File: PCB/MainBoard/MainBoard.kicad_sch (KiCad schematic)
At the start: 13 parts, among them J1 Switch, U1 MCP1700-3302E/TO, U2 ATmega4808-A

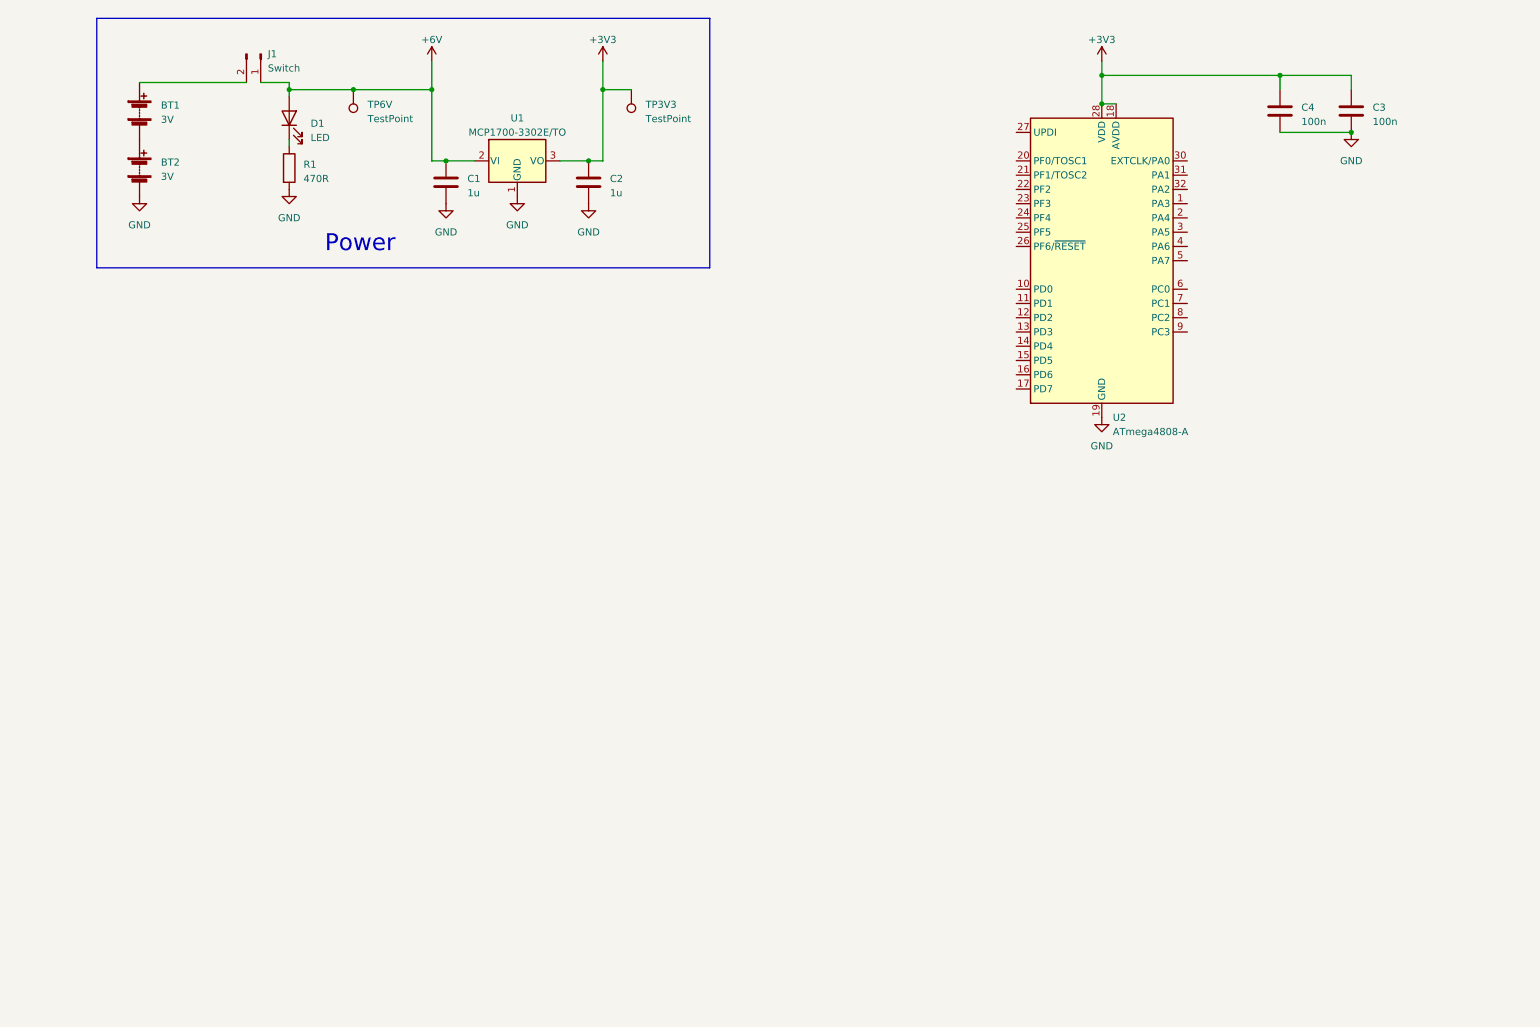
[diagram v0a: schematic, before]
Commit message: Added MCU supporting components
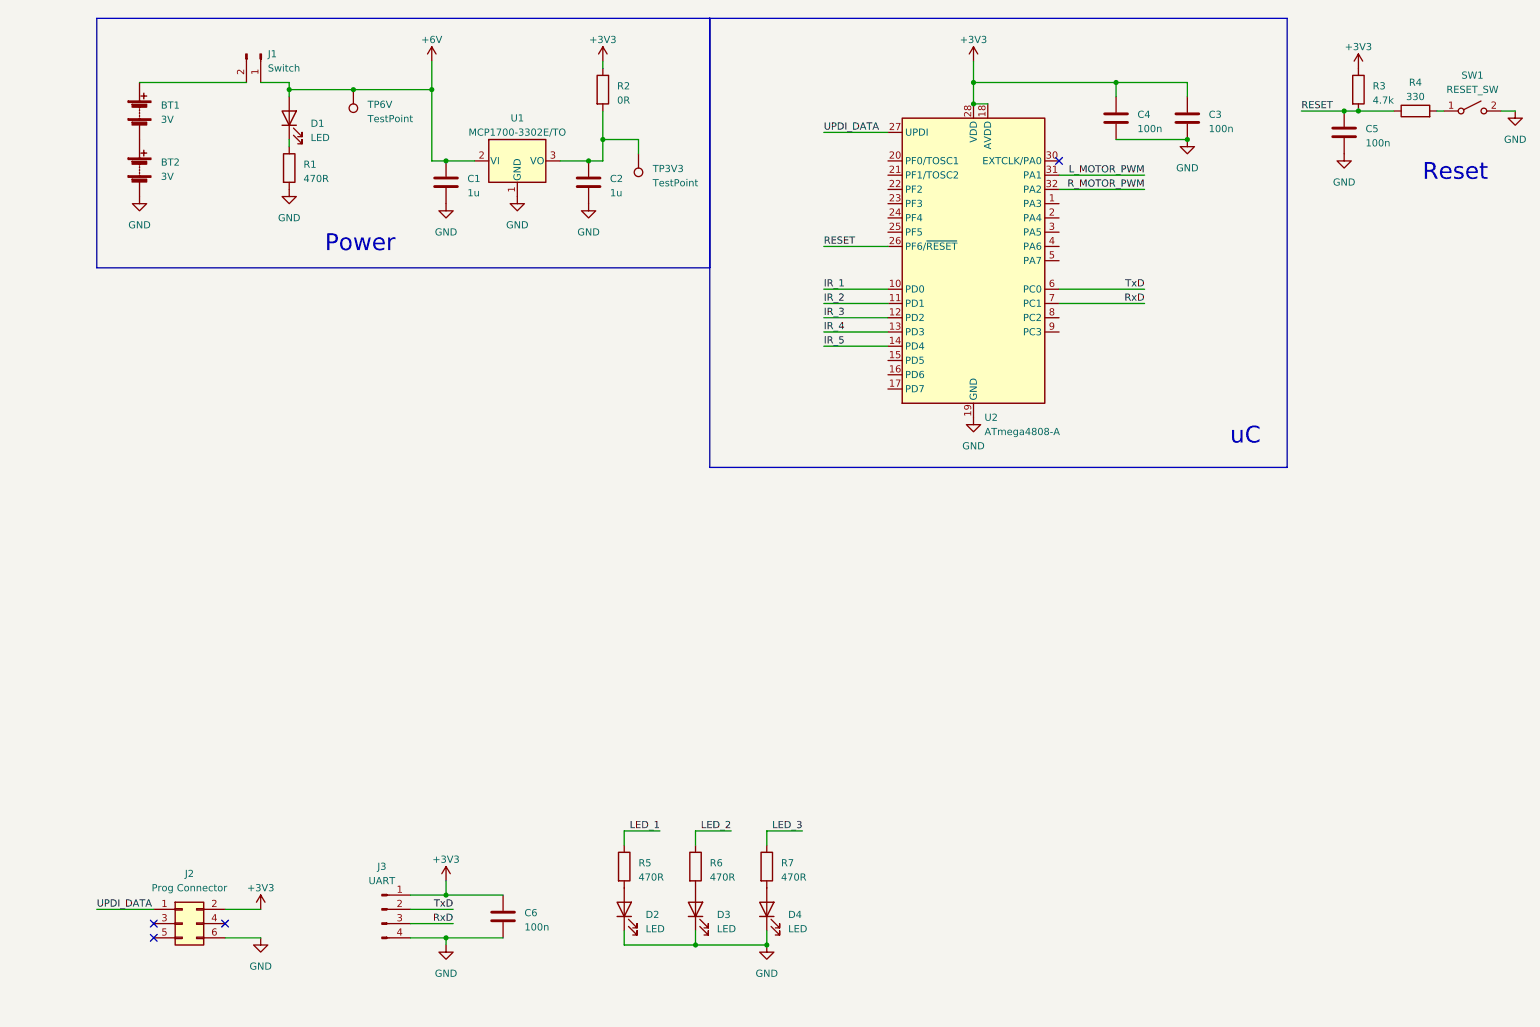
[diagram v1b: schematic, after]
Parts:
- added C5, C6: 100n, symbol Device:C
- added D2, D3, D4: LED, symbol Device:LED
- added J2: Prog Connector, symbol Connector_Generic:Conn_02x03_Odd_Even
- added J3: UART, symbol Connector:Conn_01x04_Pin
- added R2: 0R, symbol Device:R
- added R3: 4.7k, symbol Device:R
- added R4: 330, symbol Device:R
- added R5, R6, R7: 470R, symbol Device:R
- added SW1: RESET_SW, symbol Switch:SW_SPST
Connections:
- net +3V3: now also C6.1, J2.2 (Pin_2), J3.1 (Pin_1), R2.1, R3.1; no longer C2.1, TP3V3.1, U1.3 (VO)
- net GND: now also C5.2, C6.2, D2.1 (K), D3.1 (K), D4.1 (K), J2.6 (Pin_6), J3.4 (Pin_4), SW1.2 (B)
- net IR_1: now reaches U2.10 (PD0)
- net IR_2: now reaches U2.11 (PD1)
- net IR_3: now reaches U2.12 (PD2)
- net IR_4: now reaches U2.13 (PD3)
- net IR_5: now reaches U2.14 (PD4)
- net RESET: now reaches U2.26 (PF6/~{RESET})
- net RESET: now also C5.1, R3.2, R4.1
- net UPDI_DATA: now reaches U2.27 (UPDI)
- net UPDI_DATA: now also J2.1 (Pin_1)
- net L_MOTOR_PWM: now reaches U2.31 (PA1)
- net R_MOTOR_PWM: now reaches U2.32 (PA2)
- net TxD: now reaches U2.6 (PC0)
- net TxD: now also J3.2 (Pin_2)
- net RxD: now reaches U2.7 (PC1)
- net RxD: now also J3.3 (Pin_3)
- new net: C2.1, R2.2, TP3V3.1, U1.3 (VO)
- new net: R4.2, SW1.1 (A)
- new net: D4.2 (A), R7.2
- new net: D2.2 (A), R5.2
- new net: D3.2 (A), R6.2
- new net LED_1: R5.1
- new net LED_2: R6.1
- new net LED_3: R7.1
- no-connect marks 0 -> 4
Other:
- note added: "Reset"
- note added: "uC"
- moved on the sheet: C3, C4, TP3V3, U2

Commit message: Progress on Main Board
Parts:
- added J4: IR Connector, Connector_PinHeader_2.54mm:PinHeader_2x04_P2.54mm_Vertical, symbol PCM_4ms_Connector:Conn_02x04
- added J5, J6: Conn_01x02_Pin, Connector_PinHeader_2.54mm:PinHeader_1x02_P2.54mm_Vertical, symbol Connector:Conn_01x02_Pin
- BT1, BT2: footprint (none) -> Battery:BatteryHolder_Keystone_2462_2xAA
- C1, C2, C3, C4, C5, C6: footprint (none) -> Capacitor_SMD:C_1206_3216Metric
- D1, D2, D3, D4: footprint (none) -> LED_THT:LED_D5.0mm
- J1: footprint (none) -> Connector_PinHeader_2.54mm:PinHeader_1x02_P2.54mm_Vertical
- J2: footprint (none) -> Connector_PinHeader_2.54mm:PinHeader_2x03_P2.54mm_Vertical
- J3: footprint (none) -> Connector_PinHeader_2.54mm:PinHeader_1x04_P2.54mm_Vertical
- R1, R2, R3, R4, R5, R6, R7: footprint (none) -> Resistor_SMD:R_1206_3216Metric
- SW1: footprint (none) -> Button_Switch_THT:SW_PUSH_6mm
- TP3V3: footprint (none) -> TestPoint:TestPoint_Pad_D2.0mm
- TP6V1: renamed from TP6V; footprint (none) -> TestPoint:TestPoint_Pad_D2.0mm
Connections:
- net GND: now also J4.8 (Pin_8), J5.2 (Pin_2), J6.2 (Pin_2)
- net IR_1: now also J4.3 (Pin_3)
- net IR_2: now also J4.5 (Pin_5)
- net IR_3: now also J4.7 (Pin_7)
- net IR_4: now also J4.4 (Pin_4)
- net IR_5: now also J4.6 (Pin_6)
- new net L_MotorOut: J5.1 (Pin_1)
- new net R_MotorOut: J6.1 (Pin_1)
- new net VCC: J4.1 (Pin_1)
- no-connect marks 4 -> 5

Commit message: More main
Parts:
- added C7, C8: 10u, Capacitor_SMD:C_1206_3216Metric, symbol Device:C
- added D1 (x2): SB130, Diode_THT:D_DO-41_SOD81_P7.62mm_Horizontal, symbol Diode:SB130
- added J7, J8: Conn_01x02_Pin, Connector_PinHeader_2.54mm:PinHeader_1x02_P2.54mm_Vertical, symbol Connector:Conn_01x02_Pin
- added Q2 (x2): BSR802, Package_TO_SOT_SMD:SOT-23, symbol Transistor_FET:2N7002H
- added R1 (x2): 10000, Resistor_SMD:R_0805_2012Metric, symbol Device:R
- added R2 (x2): 100, Resistor_SMD:R_0805_2012Metric, symbol Device:R
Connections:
- net +6V: now also C7.1, C8.1, D1.1 (K), D1.1 (K), J7.2 (Pin_2), J8.2 (Pin_2)
- net GND: now also C7.2, C8.2, Q2.2 (S), Q2.2 (S), R1.2, R1.2
- net L_MOTOR_PWM: now also R1.1, R2.1
- net R_MOTOR_PWM: now also R1.1, R2.1
- new net: Q2.1 (G), R2.2 (x2)
- new net: D1.2 (A), J7.1 (Pin_1), Q2.3 (D)
- new net: D1.2 (A), J8.1 (Pin_1), Q2.3 (D)

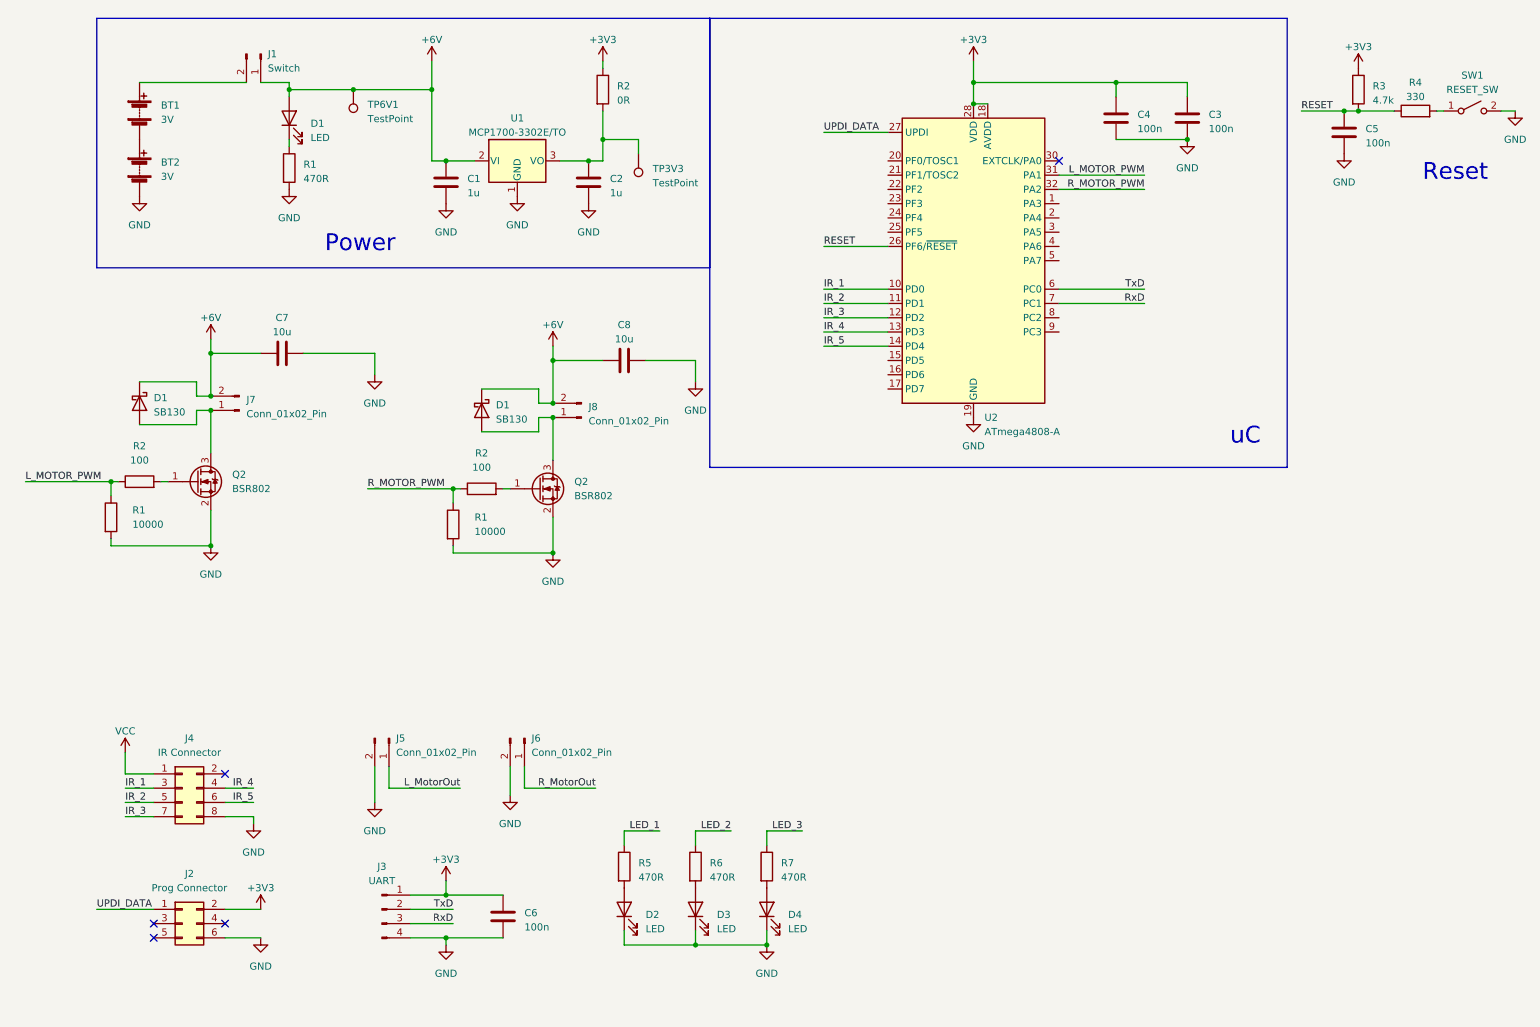
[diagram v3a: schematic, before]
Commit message: Routed main board
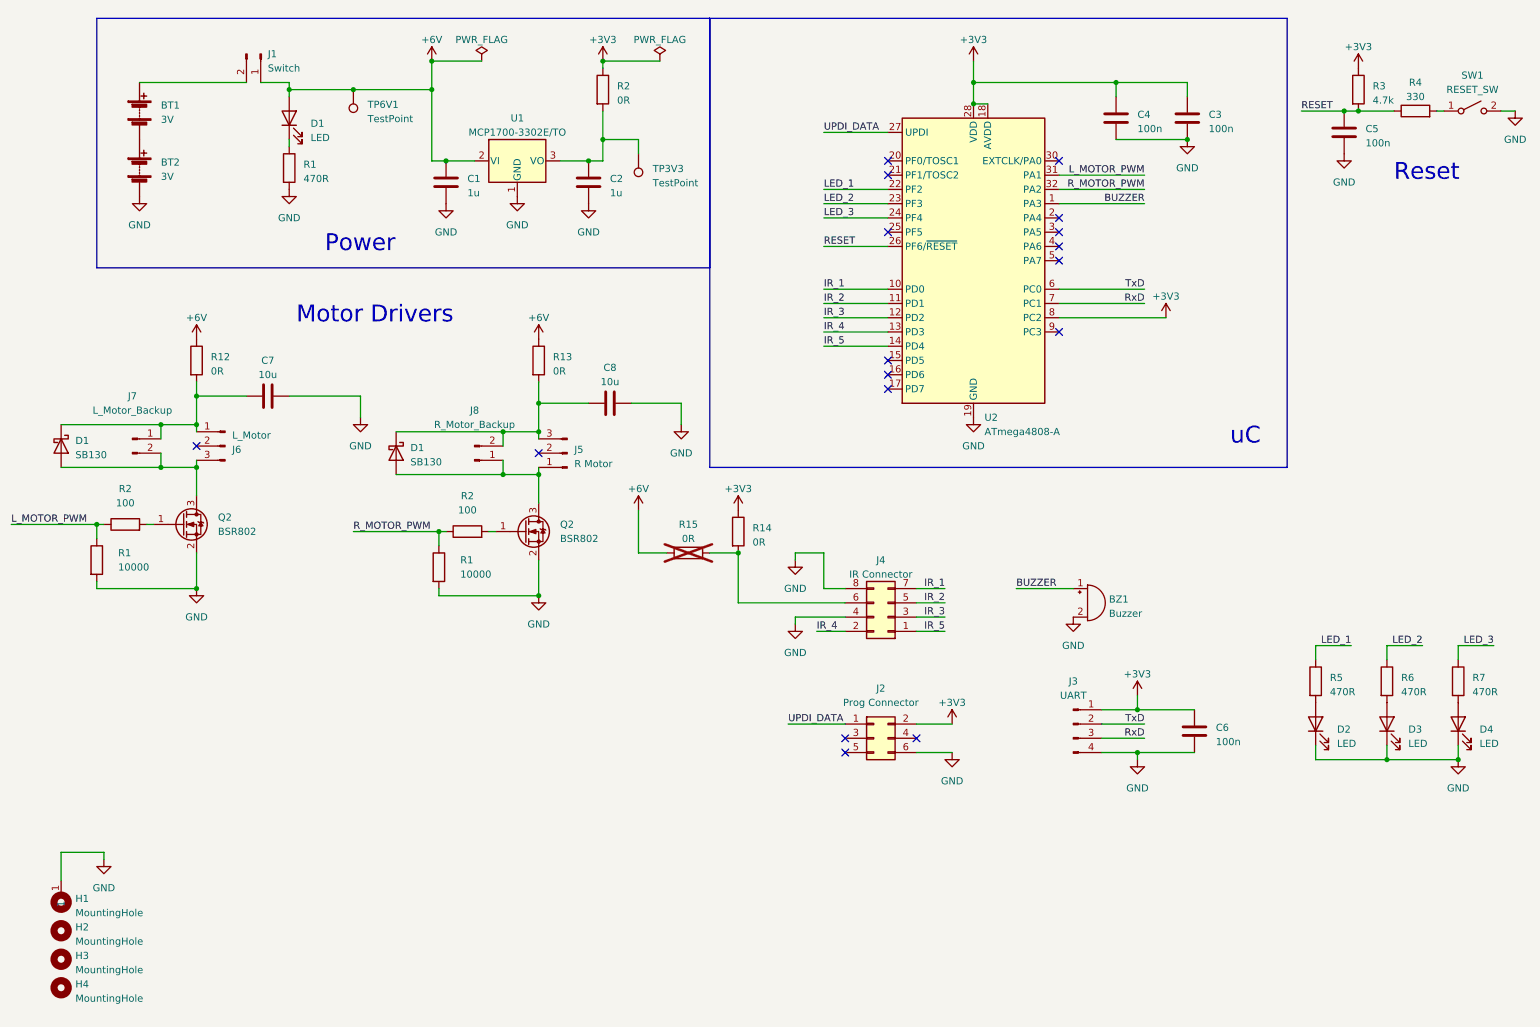
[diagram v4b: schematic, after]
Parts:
- removed J4: IR Connector, Connector_PinHeader_2.54mm:PinHeader_2x04_P2.54mm_Vertical, symbol PCM_4ms_Connector:Conn_02x04
- removed J5, J6: Conn_01x02_Pin, Connector_PinHeader_2.54mm:PinHeader_1x02_P2.54mm_Vertical, symbol Connector:Conn_01x02_Pin
- added BZ1: Buzzer, Custom:PKM13EPYH4000, symbol Device:Buzzer
- added H1, H2, H3, H4: MountingHole, MountingHole:MountingHole_3.2mm_M3_Pad_Via, symbol Mechanical:MountingHole
- added J4: IR Connector, Connector_PinHeader_2.54mm:PinHeader_2x04_P2.54mm_Vertical, symbol Connector_Generic:Conn_02x04_Odd_Even
- added J5: R Motor, Connector_JST:JST_PH_S3B-PH-K_1x03_P2.00mm_Horizontal, symbol Connector:Conn_01x03_Pin
- added J6: L_Motor, Connector_JST:JST_PH_S3B-PH-K_1x03_P2.00mm_Horizontal, symbol Connector:Conn_01x03_Pin
- added R12, R13, R14, R15: 0R, Resistor_SMD:R_0805_2012Metric, symbol Device:R
- J7: value Conn_01x02_Pin -> L_Motor_Backup
- J8: value Conn_01x02_Pin -> R_Motor_Backup
- R1, R2, R3, R4, R5, R6, R7: footprint Resistor_SMD:R_1206_3216Metric -> Resistor_SMD:R_0805_2012Metric
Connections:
- net +3V3: now also U2.8 (PC2), R14.1
- net +6V: now also R12.1, R13.1, R15.1; no longer C7.1, C8.1, D1.1 (K), D1.1 (K), J7.2 (Pin_2), J8.2 (Pin_2)
- net GND: now also BZ1.2 (+), H1.1, J4.4 (Pin_4), J4.8 (Pin_8)
- net IR_1: now also J4.7 (Pin_7)
- net IR_2: now also J4.5 (Pin_5)
- net IR_3: now also J4.3 (Pin_3)
- net IR_4: now also J4.2 (Pin_2)
- net IR_5: now also J4.1 (Pin_1)
- net LED_1: now also U2.22 (PF2)
- net LED_2: now also U2.23 (PF3)
- net LED_3: now also U2.24 (PF4)
- net at D1.2 (A), Q2.3 (D): now also J7.2 (Pin_2), J6.3 (Pin_3); no longer J7.1 (Pin_1)
- net at D1.2 (A), J8.1 (Pin_1), Q2.3 (D): now also J5.1 (Pin_1)
- net BUZZER: now reaches U2.1 (PA3)
- net BUZZER: now also BZ1.1 (-)
- new net: C8.1, D1.1 (K), J5.3 (Pin_3), J8.2 (Pin_2), R13.2
- new net: J4.6 (Pin_6), R14.2, R15.2
- new net: C7.1, D1.1 (K), J6.1 (Pin_1), J7.1 (Pin_1), R12.2
- no-connect marks 5 -> 17
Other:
- note added: "Motor Drivers"
- moved on the sheet: C6, C7, C8, D1, D2, D3, D4, J2, J3, Q2, R1, R2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

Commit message: Edits to both boards
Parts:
- added C10, C9: C, Capacitor_THT:CP_Radial_D5.0mm_P2.50mm, symbol Device:C
- added J9: Backup connector bit, Connector_PinHeader_2.00mm:PinHeader_1x05_P2.00mm_Vertical, symbol Connector:Conn_01x05_Pin
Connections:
- net +6V: now also C10.1, C9.1
- net GND: now also C10.2, C9.2
- net IR_1: now also J9.1 (Pin_1)
- net IR_2: now also J9.2 (Pin_2)
- net IR_3: now also J9.3 (Pin_3)
- net IR_4: now also J9.4 (Pin_4)
- net IR_5: now also J9.5 (Pin_5)
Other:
- moved on the sheet: BZ1, C7, R12

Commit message: Cleaned up mainboard
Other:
- note added: "Connectors"
- note added: "LED's and Buzzer"
- note added: "Misc"
- moved on the sheet: BZ1, C10, C3, C4, C5, C6, C7, C8, C9, D1, D2, D3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

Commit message: Version that was submitted
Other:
- company: (none) -> Group 28
- title: (none) -> Ankle Breaker MCU
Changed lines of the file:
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@@
 (kicad_sch (version 20230121) (generator eeschema)
   (paper "A4")
+  (title_block
+    (title "Ankle Breaker MCU")
+    (date "2023-09-22")
+    (company "Group 28")
+  )
   (junction (at 73.66 31.75) (diameter 0) (color 0 0 0 0)
   )
@@
     (effects (font (size 3 3)) (justify left bottom))
   )
-  (text "Power" (at 68.58 60.96 0)
+  (text "Power" (at 33.02 62.23 0)
     (effects (font (size 3 3)) (justify left bottom))
   )
@@
     (effects (font (size 2 2)) (justify left bottom))
   )
-  (text "uC" (at 250.19 92.71 0)
+  (text "uC" (at 163.83 97.79 0)
     (effects (font (size 3 3)) (justify left bottom))
   )
@@
     (effects (font (size 2 2)) (justify left bottom))
   )
-  (text "Motor Drivers" (at 83.82 71.12 0)
+  (text "Motor Drivers" (at 33.02 68.58 0)
     (effects (font (size 3 3)) (justify left bottom))
   )
-  (text "Connectors" (at 77.47 146.05 0)
+  (text "Connectors" (at 33.02 140.97 0)
     (effects (font (size 3 3)) (justify left bottom))
   )
